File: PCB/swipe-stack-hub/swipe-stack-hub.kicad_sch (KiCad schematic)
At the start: 60 parts, among them J1 Barrel_Jack_Switch, J2 Conn_02x08_Odd_Even, J3 Conn_02x05_Odd_Even, J4 Conn_01x06, J5 Conn_01x04, J6 Conn_01x01_Socket, J7 Conn_01x01_Socket, J8 Conn_01x01_Socket, J9 Conn_01x01_Socket, SW4 SW_Push, SW5 SW_Push, U1 STM32F091RCTx, U2 LMR51430 (LMR54410), U3 HM19R, U4 HM19L, U5 MAX7375AXR805, U6 LM386

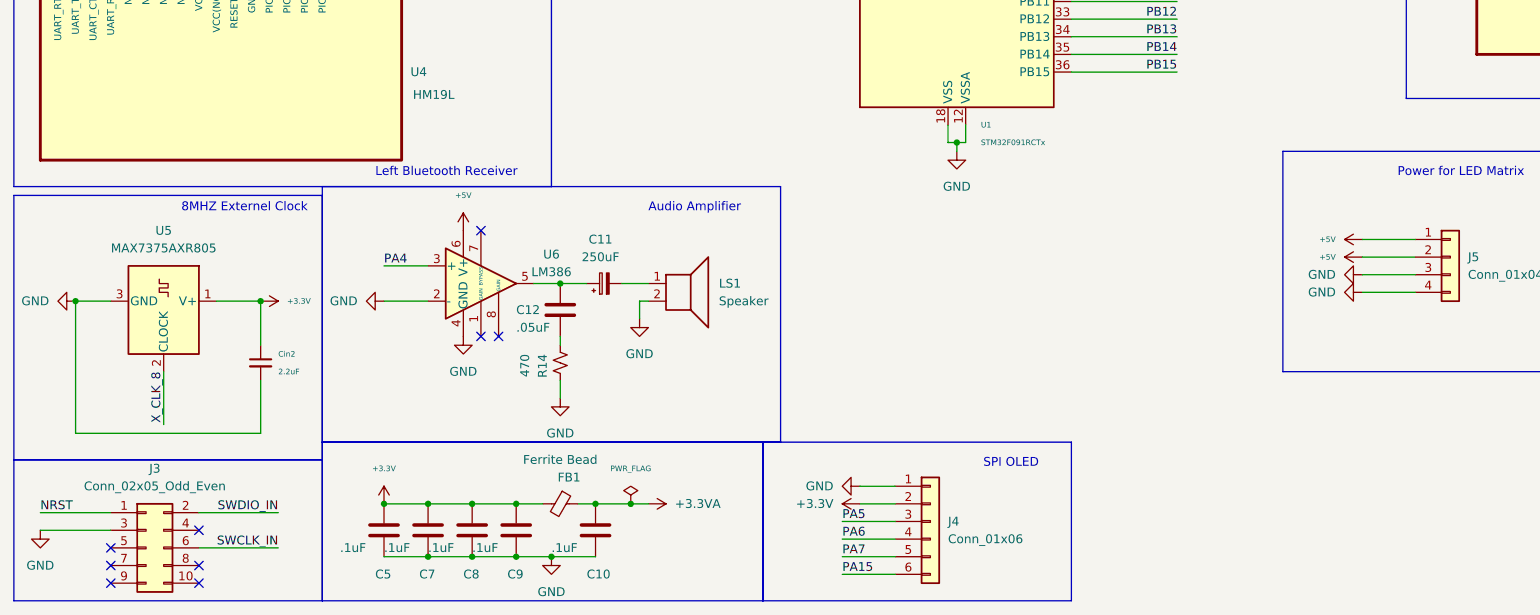
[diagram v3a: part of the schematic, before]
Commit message: changed some capacitors
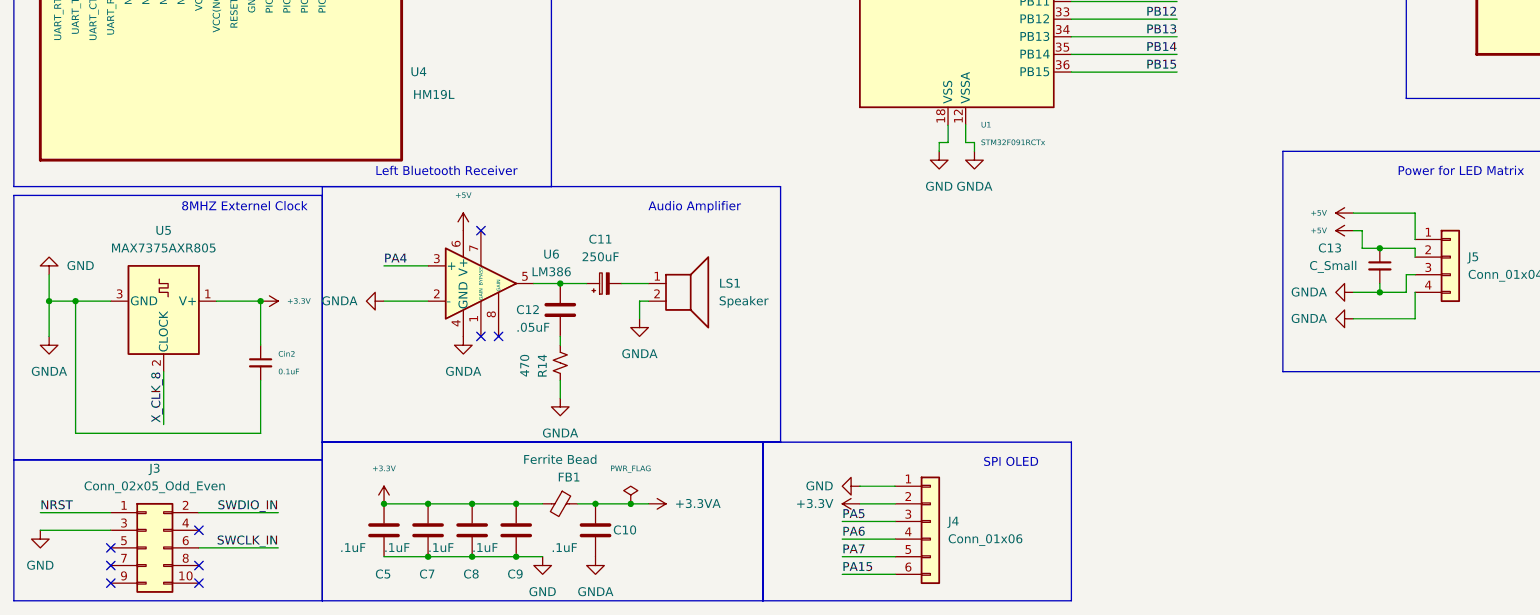
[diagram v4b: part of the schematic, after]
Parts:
- added C13: C_Small, Capacitor_THT:C_Radial_D6.3mm_H11.0mm_P2.50mm, symbol Device:C_Small
- C11: footprint Capacitor_SMD:C_0805_2012Metric_Pad1.18x1.45mm_HandSolder -> Capacitor_THT:C_Radial_D6.3mm_H7.0mm_P2.50mm
- Cin2: value 2.2uF -> 0.1uF
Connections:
- net +5V: now also C13.1
- net GND: now also C13.2

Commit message: pcb changes
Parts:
- added RN1, RN2: R_Pack08, Library:SOIC127P762X240-16N, symbol Device:R_Pack08
- C11: footprint Capacitor_THT:C_Radial_D6.3mm_H7.0mm_P2.50mm -> Capacitor_THT:CP_Radial_D14.0mm_P7.50mm
- C13: footprint Capacitor_THT:C_Radial_D6.3mm_H11.0mm_P2.50mm -> Capacitor_THT:CP_Radial_D14.0mm_P5.00mm
- Cout1: footprint Capacitor_SMD:C_0805_2012Metric_Pad1.18x1.45mm_HandSolder -> Capacitor_THT:CP_Radial_D5.0mm_P2.50mm
- J3: footprint Connector_IDC:IDC-Header_2x05_P2.54mm_Vertical_SMD -> Connector_IDC:IDC-Header_2x05_P2.54mm_Vertical
- J4: footprint Connector_JST:JST_EH_B6B-EH-A_1x06_P2.50mm_Vertical -> Connector_JST:JST_VH_B6P-VH-B_1x06_P3.96mm_Vertical
- J5: footprint Connector_JST:JST_EH_B4B-EH-A_1x04_P2.50mm_Vertical -> Connector_JST:JST_VH_B4P-VH-B_1x04_P3.96mm_Vertical
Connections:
- net A0: now also RN1.13 (R4.2); no longer J2.9 (Pin_9)
- net A1: now also RN2.4 (R4.1); no longer J2.10 (Pin_10)
- net A2: now also RN1.14 (R3.2); no longer J2.11 (Pin_11)
- net A3: now also RN2.3 (R3.1); no longer J2.12 (Pin_12)
- net A4: now also RN2.5 (R5.1); no longer J2.8 (Pin_8)
- net B0: now also U1.28 (PB2), RN1.10 (R7.2); no longer J2.3 (Pin_3), U1.56 (PB4)
- net B1: now also RN1.12 (R5.2); no longer J2.7 (Pin_7)
- net BLNK: now also RN1.16 (R1.2); no longer J2.15 (Pin_15)
- net Clk: now also RN1.15 (R2.2); no longer J2.13 (Pin_13)
- net G0: now also U1.27 (PB1), RN2.8 (R8.1); no longer J2.2 (Pin_2), U1.28 (PB2)
- net G1: now also U1.56 (PB4), RN2.6 (R6.1); no longer J2.6 (Pin_6), U1.55 (PB3)
- net GND: now also RN2.1 (R1.1), RN2.7 (R7.1); no longer J2.16 (Pin_16), J2.4 (Pin_4)
- net LAT: now also RN2.2 (R2.1); no longer J2.14 (Pin_14)
- net PB0: now also RN1.9 (R8.2); no longer J2.1 (Pin_1)
- net PB1: no longer names the net of J2.5 (Pin_5)
- net PB1: now also RN1.6 (R6.1); no longer U1.27 (PB1)
- new net: J2.15 (Pin_15), RN1.1 (R1.1)
- new net: J2.13 (Pin_13), RN1.2 (R2.1)
- new net: J2.11 (Pin_11), RN1.3 (R3.1)
- new net: J2.9 (Pin_9), RN1.4 (R4.1)
- new net: J2.7 (Pin_7), RN1.5 (R5.1)
- new net: J2.3 (Pin_3), RN1.7 (R7.1)
- new net: J2.1 (Pin_1), RN1.8 (R8.1)
- new net: J2.4 (Pin_4), RN2.10 (R7.2)
- new net: J2.6 (Pin_6), RN2.11 (R6.2)
- new net: J2.8 (Pin_8), RN2.12 (R5.2)
- new net: J2.10 (Pin_10), RN2.13 (R4.2)
- new net: J2.12 (Pin_12), RN2.14 (R3.2)
- new net: J2.14 (Pin_14), RN2.15 (R2.2)
- new net: J2.16 (Pin_16), RN2.16 (R1.2)
- new net: J2.2 (Pin_2), RN2.9 (R8.2)
- new net PB3: RN1.11 (R6.2), U1.55 (PB3)
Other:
- moved on the sheet: C13, J2, J5

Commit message: uhhhhhh
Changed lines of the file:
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@@
   (junction (at 246.38 78.74) (diameter 0) (color 0 0 0 0)
   )
+  (junction (at 96.52 191.77) (diameter 0) (color 0 0 0 0)
+  )
   (junction (at 147.32 33.02) (diameter 0) (color 0 0 0 0)
   )
@@
     )
   )
+  (symbol (lib_id "power:GNDA") (at 102.87 157.48 0) (unit 1)
+    (in_bom yes) (on_board yes) (dnp no) (fields_autoplaced)
+    (property "Reference" "#PWR046" (at 102.87 163.83 0)
+      (effects (font (size 1.27 1.27)) hide)
+    )
+    (property "Value" "GNDA" (at 102.87 162.56 0)
+      (effects (font (size 1.27 1.27)))
+    )
+    (property "Footprint" "" (at 102.87 157.48 0)
+      (effects (font (size 1.27 1.27)) hide)
+    )
+    (property "Datasheet" "" (at 102.87 157.48 0)
+      (effects (font (size 1.27 1.27)) hide)
+    )
+    (pin "1")
+    (instances
+      (project "swipe-stack-hub"
+        (path "/2a19c3a6-698c-4845-b3c3-139632a3e17c"
+          (reference "#PWR046") (unit 1)
+        )
+      )
+    )
+  )
   (symbol (lib_id "power:GND") (at 34.29 26.67 90) (unit 1)
     (in_bom yes) (on_board yes) (dnp no) (fields_autoplaced)
@@
     )
   )
+  (symbol (lib_id "power:PWR_FLAG") (at 96.52 191.77 270) (unit 1)
+    (in_bom yes) (on_board yes) (dnp no) (fields_autoplaced)
+    (property "Reference" "#FLG05" (at 98.425 191.77 0)
+      (effects (font (size 1.27 1.27)) hide)
+    )
+    (property "Value" "PWR_FLAG" (at 100.33 191.77 90)
+      (effects (font (size 1.27 1.27)) (justify left))
+    )
+    (property "Footprint" "" (at 96.52 191.77 0)
+      (effects (font (size 1.27 1.27)) hide)
+    )
+    (property "Datasheet" "~" (at 96.52 191.77 0)
+      (effects (font (size 1.27 1.27)) hide)
+    )
+    (pin "1")
+    (instances
+      (project "swipe-stack-hub"
+        (path "/2a19c3a6-698c-4845-b3c3-139632a3e17c"
+          (reference "#FLG05") (unit 1)
+        )
+      )
+    )
+  )
   (symbol (lib_id "Device:C_Polarized_Small") (at 97.79 152.4 90) (unit 1)
     (in_bom yes) (on_board yes) (dnp no) (fields_autoplaced)
@@
         )
       )
-    )
-  )
-  (symbol (lib_id "power:GNDA") (at 102.87 157.48 0) (unit 1)
-    (in_bom yes) (on_board yes) (dnp no) (fields_autoplaced)
-    (property "Reference" "#PWR046" (at 102.87 163.83 0)
-      (effects (font (size 1.27 1.27)) hide)
-    )
-    (property "Value" "GNDA" (at 102.87 162.56 0)
-      (effects (font (size 1.27 1.27)))
-    )
-    (property "Footprint" "" (at 102.87 157.48 0)
-      (effects (font (size 1.27 1.27)) hide)
-    )
-    (property "Datasheet" "" (at 102.87 157.48 0)
-      (effects (font (size 1.27 1.27)) hide)
-    )
-    (pin "1")
-    (instances
-      (project "swipe-stack-hub"
-        (path "/2a19c3a6-698c-4845-b3c3-139632a3e17c"
-          (reference "#PWR046") (unit 1)
-        )
-      )
